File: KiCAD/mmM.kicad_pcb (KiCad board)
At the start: 2 copper layers, 99 x 80 mm, 157 parts, among them J1 5V_EXT, J2 3V3_EXT, P1 AREF, P10 C3SB, P11 VSel_Vlv, P13 PWR_IN, P14 X_VALVE, P17 PUMP, P24 PWR_IN, P34 VSel_Vlv2, P38 X_VALVE2, P4 ICSP, P5 FTDI, P7 GAGE_PR, P9 C3SB, Q1 BCP5416TA, Q2 BCP5416TA, Q3 BCP5416TA, Q4 BCP5416TA, SW1 Reset, SW2 INT0, SW3 INT1, U1 TXB0104D, U2 LM2675-5.0, U3 LM2675-3.3, U5 DS3231N, U7 ATMEGA328-AU-ND, X1 16MHz

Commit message: Fresh BOM for mmM
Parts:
- C1, C4: value 100n -> 100nF
- U7: value ATMEGA328-AU-ND -> ATMEGA328P-AU-ND
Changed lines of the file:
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@@
     (links 301)
     (no_connects 0)
-    (area 13.936499 13.936499 113.063501 94.063501)
+    (area 13.085 13.899999 126.418668 101.828801)
     (thickness 1.6)
     (drawings 136)
@@
   )
   (layers
-    (0 F.Cu signal)
-    (31 B.Cu signal)
+    (0 F.Cu signal hide)
+    (31 B.Cu signal hide)
     (32 B.Adhes user)
     (33 F.Adhes user)
@@
       (effects (font (size 0.8 0.8) (thickness 0.12)))
     )
-    (fp_text value ATMEGA328-AU-ND (at 0 1.905) (layer F.SilkS) hide
+    (fp_text value ATMEGA328P-AU-ND (at 0 1.905) (layer F.SilkS) hide
       (effects (font (size 0.8 0.8) (thickness 0.12)))
     )
@@
       (effects (font (size 0.8 0.8) (thickness 0.12)))
     )
-    (fp_text value 100n (at 0 1.7145 180) (layer F.SilkS) hide
+    (fp_text value 100nF (at 0 1.7145 180) (layer F.SilkS) hide
       (effects (font (size 0.8 0.8) (thickness 0.12)))
     )
@@
       (effects (font (size 0.8 0.8) (thickness 0.12)))
     )
-    (fp_text value 100n (at 0 1.7145 90) (layer F.SilkS) hide
+    (fp_text value 100nF (at 0 1.7145 90) (layer F.SilkS) hide
       (effects (font (size 0.8 0.8) (thickness 0.12)))
     )

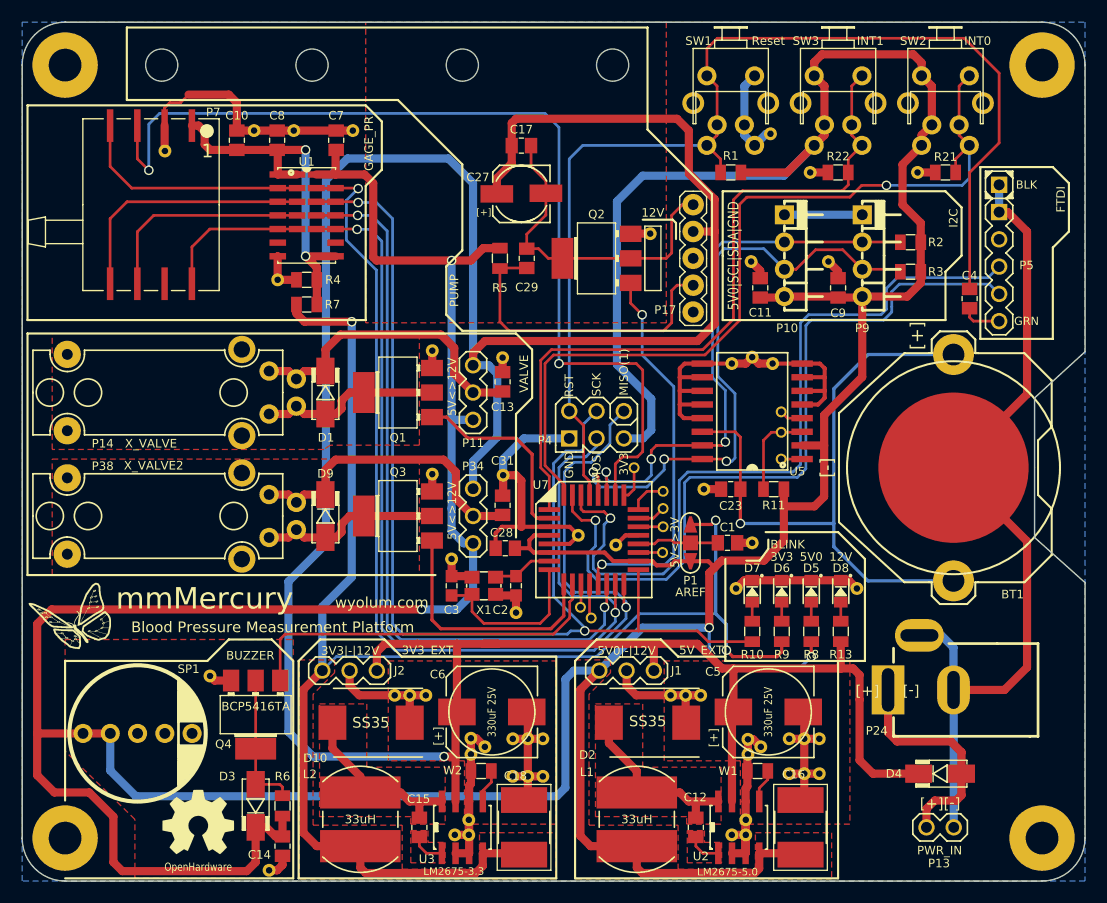
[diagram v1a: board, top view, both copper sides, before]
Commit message: added pull down resistors on microcontroller outputs
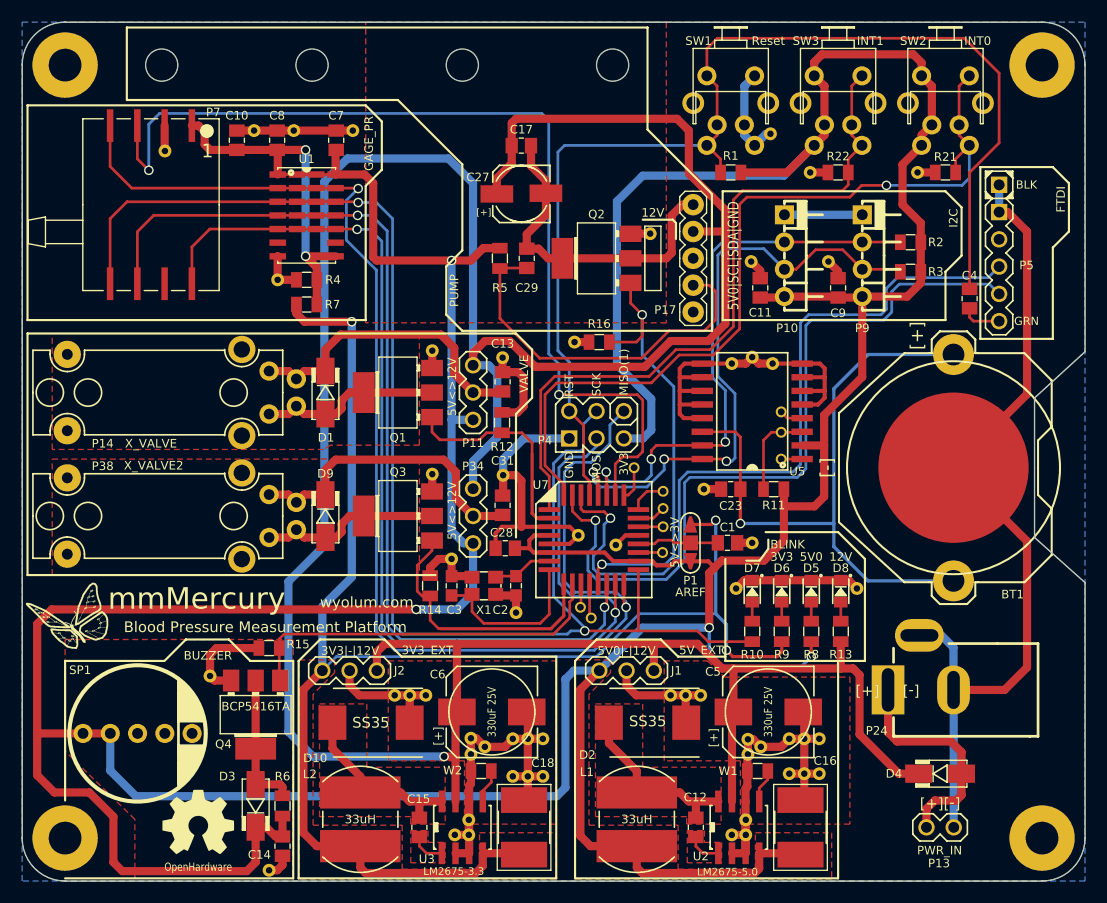
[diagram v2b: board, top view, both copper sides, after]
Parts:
- added R12: 10k, mmM:r_0805, F.Cu at (58.7, 51.3)
- added R14: 10k, mmM:r_0805, F.Cu at (52.0, 66.5)
- added R15: 10k, mmM:r_0805, F.Cu at (37.0, 72.3)
- added R16: 10k, mmM:r_0805, F.Cu at (67.8, 43.8)
- added REF59: via01, uCm:via_th, F.Cu at (65.5, 43.8)
- moved G2 0.26 mm to (13.2, 65.7)
- renumbered REF** to REF1, REF** to REF10, REF** to REF11, REF** to REF12, REF** to REF13, REF** to REF14, REF** to REF15, REF** to REF16, REF** to REF17, REF** to REF18, REF** to REF19, REF** to REF2, REF** to REF20, REF** to REF21, REF** to REF22, REF** to REF23, REF** to REF24, REF** to REF25, REF** to REF26, REF** to REF27, REF** to REF28, REF** to REF29, REF** to REF3, REF** to REF30, REF** to REF31, REF** to REF32, REF** to REF33, REF** to REF34, REF** to REF35, REF** to REF36, REF** to REF37, REF** to REF38, REF** to REF39, REF** to REF4, REF** to REF40, REF** to REF41, REF** to REF42, REF** to REF43, REF** to REF44, REF** to REF45, REF** to REF46, REF** to REF47, REF** to REF48, REF** to REF49, REF** to REF5, REF** to REF50, REF** to REF51, REF** to REF52, REF** to REF53, REF** to REF54, REF** to REF55, REF** to REF56, REF** to REF57, REF** to REF58, REF** to REF6, REF** to REF7, REF** to REF8, REF** to REF9
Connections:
- C10 pad 1: /Interface/3V3_PR -> /Interface/5V0
- C8 pad 1: /Interface/3V3_PR -> /Interface/5V0
- P17 pad 3: Net-(P17-Pad3) -> (no net)
- P17 pad 5: Net-(P17-Pad5) -> (no net)
- P5 pad 3: Net-(P5-Pad3) -> (no net)
- P7 pad 1: /Interface/3V3_PR -> /Interface/5V0
- P7 pad 4: /Interface/P_MISO -> /Interface/MISO
- P7 pad 5: /Interface/P_SCK -> /Interface/SCK
- P7 pad 6: /Interface/P_SS -> /Interface/~SS
- P7 pad 7: Net-(P7-Pad7) -> (no net)
- P7 pad 8: /Interface/P_MOSI -> /Interface/~MOSI
- R4 pad 2: /Interface/3V3_PR -> /Interface/5V0
- R7 pad 2: /Interface/3V3_PR -> /Interface/5V0
- U1 pad 1: /Interface/3V3_PR -> /Interface/5V0
- U1 pad 2: /Interface/P_MISO -> /Interface/MISO
- U1 pad 3: /Interface/P_SCK -> /Interface/SCK
- U1 pad 4: /Interface/P_SS -> /Interface/~SS
- U1 pad 5: /Interface/P_MOSI -> /Interface/~MOSI
- U1 pad 6: Net-(U1-Pad6) -> (no net)
- U1 pad 8: /Interface/3V3_PR -> /Interface/5V0
- U1 pad 9: Net-(U1-Pad9) -> (no net)
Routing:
- net /Interface/5V0: track 465.4 -> 501.1 mm, vias 4 -> 6
- net /Interface/3V3_PR: track 34.0 -> 0.00 mm, vias 2 -> 0
- net /Interface/SCK: track 109.8 -> 135.7 mm
- net /Interface/P_SCK: track 24.1 -> 0.00 mm
- net /Interface/MISO: track 101.4 -> 125.3 mm
- net /Interface/~SS: track 69.2 -> 91.3 mm
- net /Interface/P_MISO: track 22.1 -> 0.00 mm
- net /Interface/P_SS: track 20.4 -> 0.00 mm
- net /Interface/~MOSI: track 92.1 -> 107.8 mm
- net /Interface/P_MOSI: track 13.9 -> 0.00 mm
- net GND: track 320.5 -> 332.9 mm
- net /Interface/Pump: track 29.3 -> 35.2 mm
- net /Interface/~PB1_Pump: track 36.1 -> 41.4 mm
- net /Interface/PD4_Valve2: track 18.0 -> 20.0 mm
- net /RESET: track 108.5 -> 110.4 mm
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
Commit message: mods to board layout
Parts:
- moved REF39 5.66 mm to (84.3, 41.4)
- moved REF38 5.15 mm to (88.4, 41.4)
- moved C11 1.75 mm to (82.8, 40.5), turned to 90 degrees
- moved C9 1.75 mm to (90.0, 40.5), turned to 90 degrees
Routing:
- net GND: track 332.9 -> 869.5 mm
- net /Interface/PC3_Pr1: track 91.5 -> 96.6 mm
- net /Interface/SCL: track 57.7 -> 54.5 mm
- net /RESET: track 110.4 -> 107.5 mm
- net /RXD: track 72.7 -> 69.9 mm
- net /TXD: track 72.6 -> 69.8 mm
- net /Interface/SDA: track 53.0 -> 52.4 mm
